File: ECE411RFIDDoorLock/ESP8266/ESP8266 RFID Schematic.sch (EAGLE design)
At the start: 30 parts, among them M1 SERVO, Q3 DMG341, T1 600mA/40V, T2 600mA/40V, U3 AP2112-3.3, X1 ESP-12E, X4 20329

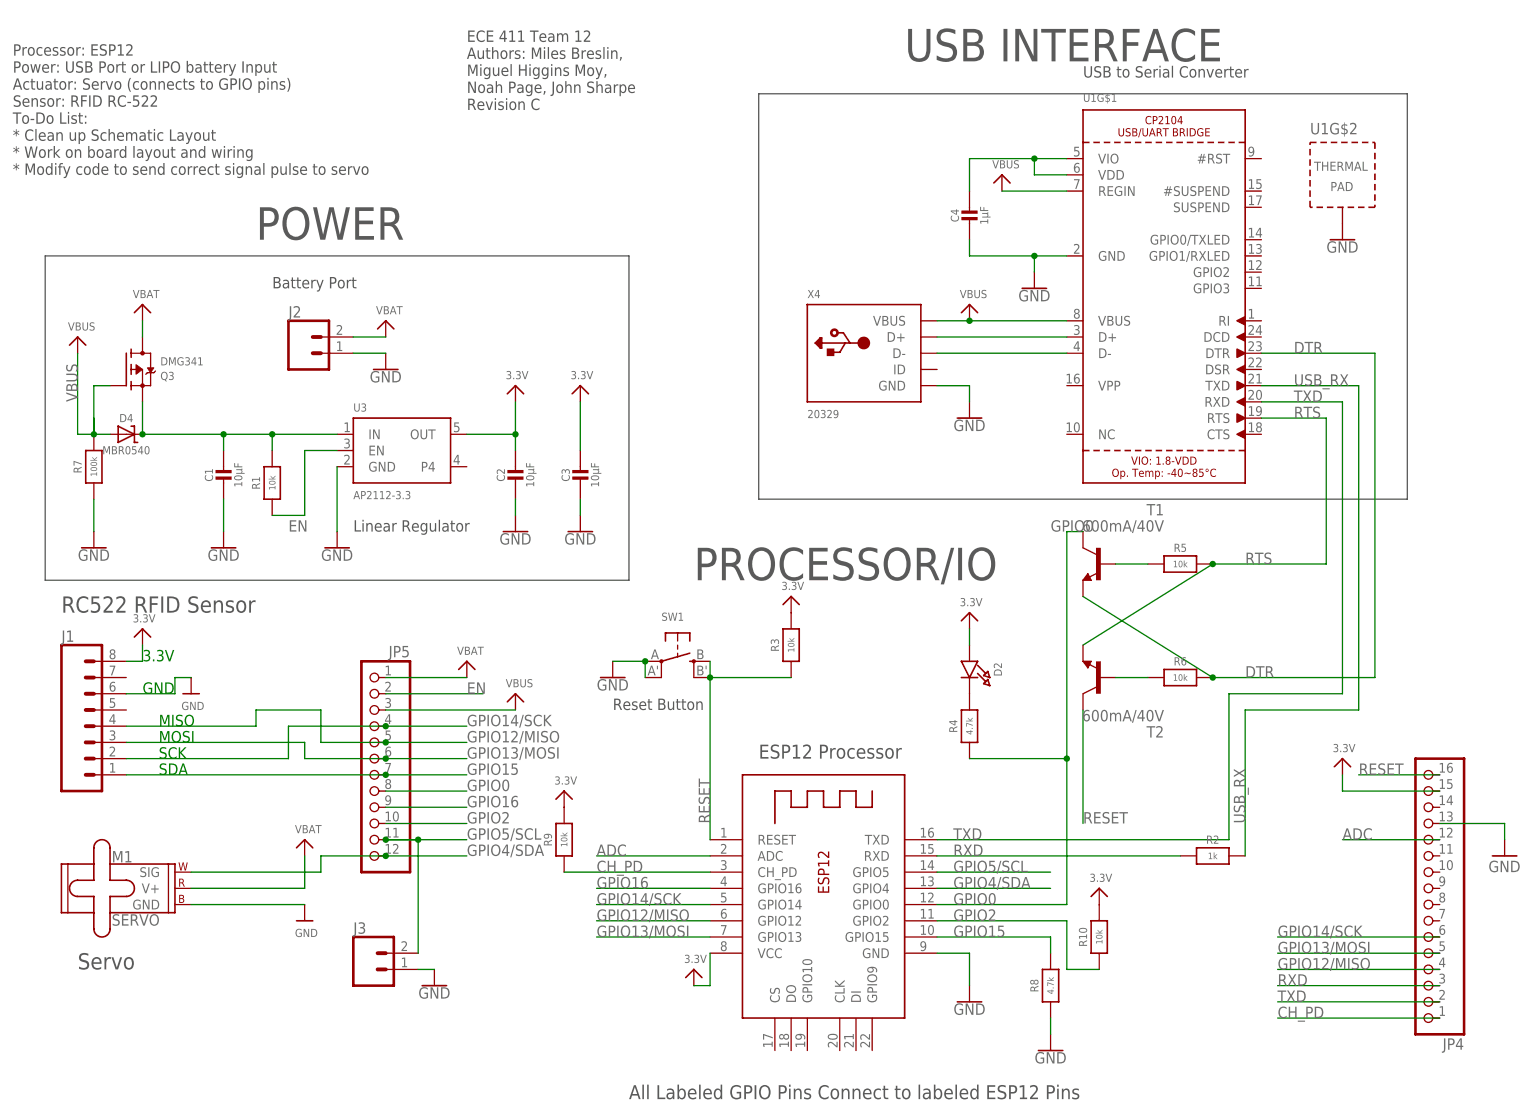
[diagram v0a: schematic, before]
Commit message: Design review feedback changed, USB replaced add new library
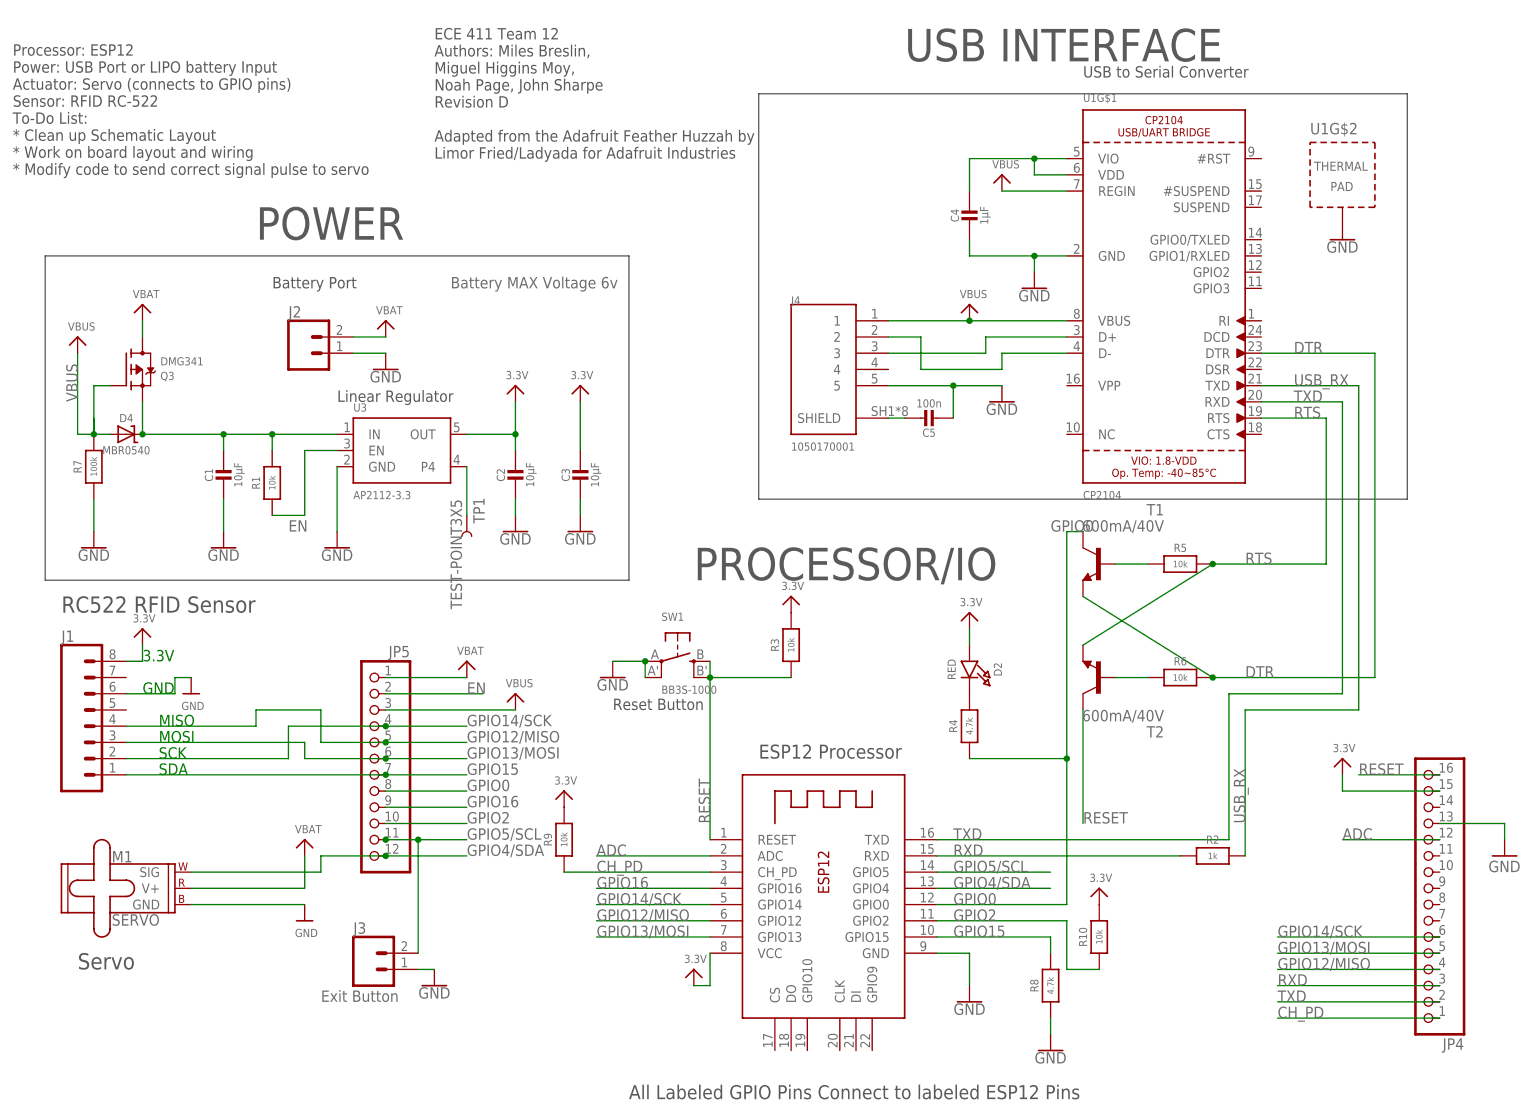
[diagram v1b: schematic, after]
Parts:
- removed X4: 20329, microbuilder:USB_MICRO_20329_V2
- added C5: 100n, microbuilder:CAP_CERAMIC0603MINI
- added J4: 1050170001, 1050170001:1050170001
- added TP1: TEST-POINT3X5, SparkFun-Connectors:TEST-POINT3X5
- D2: value (none) -> RED
- SW1: value (none) -> BB3S-1000
- U1: value (none) -> CP2104
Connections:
- new net N$1: C5.1, J4.SHIELD
- new net N$2: J4.3, U1G$1.D+
- net GND: now also C5.2, J4.5; no longer X4.GND
- net N$3: now also J4.2, U1G$1.D-; no longer U1G$1.D+, X4.D+
- net N$4: now also TP1.1, U3.P4; no longer U1G$1.D-, X4.D-
- net VBUS: now also J4.1; no longer X4.VBUS
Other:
- note added: "Battery MAX Voltage 6v"
- note added: "ECE 411 Team 12 Authors: Miles Breslin, Miguel Higgins Moy, Noah Page, John Sharpe Revision D Adapted from the Adafruit Feather Huzzah by Limor Fried/Ladyada for Adafruit Industries"
- note added: "Exit Button"
- note removed: "ECE 411 Team 12 Authors: Miles Breslin, Miguel Higgins Moy, Noah Page, John Sharpe Revision C"

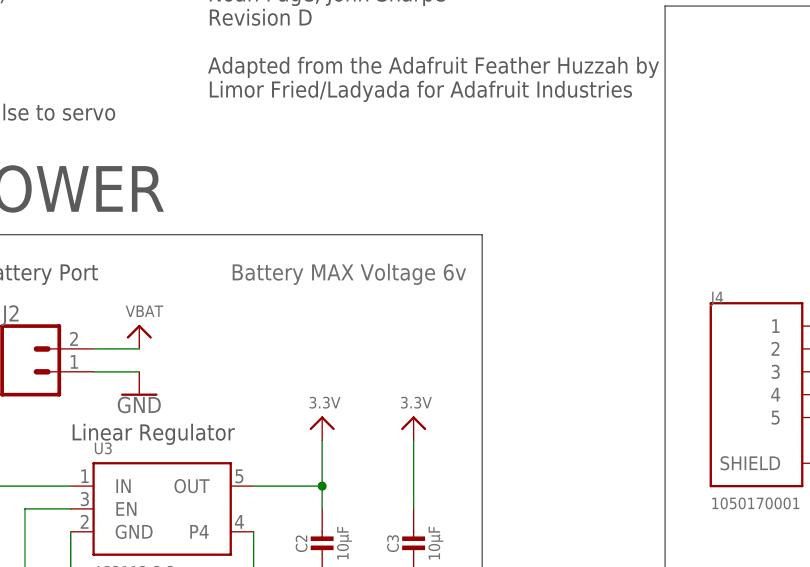
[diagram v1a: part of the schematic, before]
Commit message: PCB Clean Up from Design Review
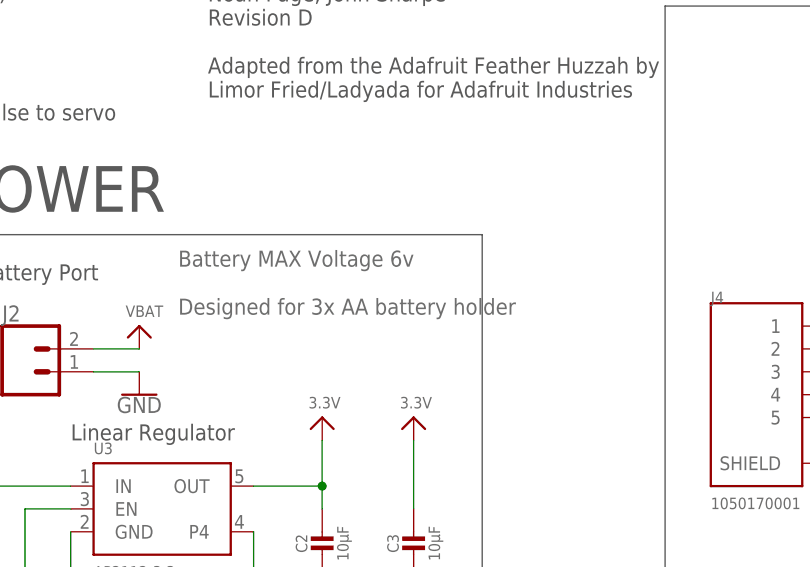
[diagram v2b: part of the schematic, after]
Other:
- note added: "Battery MAX Voltage 6v Designed for 3x AA battery holder"
- note removed: "Battery MAX Voltage 6v"
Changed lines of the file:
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@@
 <grid distance="0.1" unitdist="inch" unit="inch" style="lines" multiple="1" display="no" altdistance="0.01" altunitdist="inch" altunit="inch"/>
 <layers>
-<layer number="1" name="Top" color="4" fill="1" visible="yes" active="no"/>
-<layer number="2" name="Route2" color="16" fill="1" visible="yes" active="no"/>
-<layer number="3" name="Route3" color="17" fill="1" visible="yes" active="no"/>
-<layer number="4" name="Route4" color="18" fill="1" visible="yes" active="no"/>
-<layer number="5" name="Route5" color="19" fill="1" visible="yes" active="no"/>
-<layer number="6" name="Route6" color="25" fill="1" visible="yes" active="no"/>
-<layer number="7" name="Route7" color="26" fill="1" visible="yes" active="no"/>
-<layer number="8" name="Route8" color="27" fill="1" visible="yes" active="no"/>
-<layer number="9" name="Route9" color="28" fill="1" visible="yes" active="no"/>
-<layer number="10" name="Route10" color="29" fill="1" visible="yes" active="no"/>
-<layer number="11" name="Route11" color="30" fill="1" visible="yes" active="no"/>
-<layer number="12" name="Route12" color="20" fill="1" visible="yes" active="no"/>
-<layer number="13" name="Route13" color="21" fill="1" visible="yes" active="no"/>
-<layer number="14" name="Route14" color="22" fill="1" visible="yes" active="no"/>
-<layer number="15" name="Route15" color="23" fill="1" visible="yes" active="no"/>
-<layer number="16" name="Bottom" color="1" fill="1" visible="yes" active="no"/>
-<layer number="17" name="Pads" color="2" fill="1" visible="yes" active="no"/>
-<layer number="18" name="Vias" color="2" fill="1" visible="yes" active="no"/>
-<layer number="19" name="Unrouted" color="6" fill="1" visible="yes" active="no"/>
-<layer number="20" name="Dimension" color="24" fill="1" visible="yes" active="no"/>
-<layer number="21" name="tPlace" color="7" fill="1" visible="yes" active="no"/>
-<layer number="22" name="bPlace" color="7" fill="1" visible="yes" active="no"/>
-<layer number="23" name="tOrigins" color="15" fill="1" visible="yes" active="no"/>
-<layer number="24" name="bOrigins" color="15" fill="1" visible="yes" active="no"/>
-<layer number="25" name="tNames" color="7" fill="1" visible="yes" active="no"/>
-<layer number="26" name="bNames" color="7" fill="1" visible="yes" active="no"/>
-<layer number="27" name="tValues" color="7" fill="1" visible="yes" active="no"/>
-<layer number="28" name="bValues" color="7" fill="1" visible="yes" active="no"/>
+<layer number="1" name="Top" color="4" fill="1" visible="no" active="no"/>
+<layer number="2" name="Route2" color="16" fill="1" visible="no" active="no"/>
+<layer number="3" name="Route3" color="17" fill="1" visible="no" active="no"/>
+<layer number="4" name="Route4" color="18" fill="1" visible="no" active="no"/>
+<layer number="5" name="Route5" color="19" fill="1" visible="no" active="no"/>
+<layer number="6" name="Route6" color="25" fill="1" visible="no" active="no"/>
+<layer number="7" name="Route7" color="26" fill="1" visible="no" active="no"/>
+<layer number="8" name="Route8" color="27" fill="1" visible="no" active="no"/>
+<layer number="9" name="Route9" color="28" fill="1" visible="no" active="no"/>
+<layer number="10" name="Route10" color="29" fill="1" visible="no" active="no"/>
+<layer number="11" name="Route11" color="30" fill="1" visible="no" active="no"/>
+<layer number="12" name="Route12" color="20" fill="1" visible="no" active="no"/>
+<layer number="13" name="Route13" color="21" fill="1" visible="no" active="no"/>
+<layer number="14" name="Route14" color="22" fill="1" visible="no" active="no"/>
+<layer number="15" name="Route15" color="23" fill="1" visible="no" active="no"/>
+<layer number="16" name="Bottom" color="1" fill="1" visible="no" active="no"/>
+<layer number="17" name="Pads" color="2" fill="1" visible="no" active="no"/>
+<layer number="18" name="Vias" color="2" fill="1" visible="no" active="no"/>
+<layer number="19" name="Unrouted" color="6" fill="1" visible="no" active="no"/>
+<layer number="20" name="Dimension" color="24" fill="1" visible="no" active="no"/>
+<layer number="21" name="tPlace" color="7" fill="1" visible="no" active="no"/>
+<layer number="22" name="bPlace" color="7" fill="1" visible="no" active="no"/>
+<layer number="23" name="tOrigins" color="15" fill="1" visible="no" active="no"/>
+<layer number="24" name="bOrigins" color="15" fill="1" visible="no" active="no"/>
+<layer number="25" name="tNames" color="7" fill="1" visible="no" active="no"/>
+<layer number="26" name="bNames" color="7" fill="1" visible="no" active="no"/>
+<layer number="27" name="tValues" color="7" fill="1" visible="no" active="no"/>
+<layer number="28" name="bValues" color="7" fill="1" visible="no" active="no"/>
 <layer number="29" name="tStop" color="7" fill="3" visible="no" active="no"/>
 <layer number="30" name="bStop" color="7" fill="6" visible="no" active="no"/>
@@
 <layer number="35" name="tGlue" color="7" fill="4" visible="no" active="no"/>
 <layer number="36" name="bGlue" color="7" fill="5" visible="no" active="no"/>
-<layer number="37" name="tTest" color="7" fill="1" visible="yes" active="no"/>
-<layer number="38" name="bTest" color="7" fill="1" visible="yes" active="no"/>
+<layer number="37" name="tTest" color="7" fill="1" visible="no" active="no"/>
+<layer number="38" name="bTest" color="7" fill="1" visible="no" active="no"/>
 <layer number="39" name="tKeepout" color="4" fill="11" visible="no" active="no"/>
 <layer number="40" name="bKeepout" color="1" fill="11" visible="no" active="no"/>
@@
 <layer number="44" name="Drills" color="7" fill="1" visible="no" active="no"/>
 <layer number="45" name="Holes" color="7" fill="1" visible="no" active="no"/>
-<layer number="46" name="Milling" color="3" fill="1" visible="yes" active="no"/>
-<layer number="47" name="Measures" color="7" fill="1" visible="yes" active="no"/>
-<layer number="48" name="Document" color="7" fill="1" visible="yes" active="no"/>
-<layer number="49" name="Reference" color="7" fill="1" visible="yes" active="no"/>
-<layer number="50" name="dxf" color="7" fill="1" visible="yes" active="no"/>
-<layer number="51" name="tDocu" color="7" fill="1" visible="yes" active="no"/>
-<layer number="52" name="bDocu" color="7" fill="1" visible="yes" active="no"/>
-<layer number="53" name="tGND_GNDA" color="7" fill="9" visible="yes" active="no"/>
-<layer number="54" name="bGND_GNDA" color="1" fill="9" visible="yes" active="no"/>
-<layer number="56" name="wert" color="7" fill="1" visible="yes" active="no"/>
-<layer number="57" name="tCAD" color="7" fill="1" visible="yes" active="no"/>
-<layer number="58" name="b3D" color="7" fill="1" visible="yes" active="no"/>
-<layer number="59" name="tCarbon" color="7" fill="1" visible="yes" active="no"/>
-<layer number="60" name="bCarbon" color="7" fill="1" visible="yes" active="no"/>
-<layer number="61" name="stand" color="7" fill="1" visible="yes" active="no"/>
+<layer number="46" name="Milling" color="3" fill="1" visible="no" active="no"/>
+<layer number="47" name="Measures" color="7" fill="1" visible="no" active="no"/>
+<layer number="48" name="Document" color="7" fill="1" visible="no" active="no"/>
+<layer number="49" name="Reference" color="7" fill="1" visible="no" active="no"/>
+<layer number="50" name="dxf" color="7" fill="1" visible="no" active="no"/>
+<layer number="51" name="tDocu" color="7" fill="1" visible="no" active="no"/>
+<layer number="52" name="bDocu" color="7" fill="1" visible="no" active="no"/>
+<layer number="53" name="tGND_GNDA" color="7" fill="9" visible="no" active="no"/>
+<layer number="54" name="bGND_GNDA" color="1" fill="9" visible="no" active="no"/>
+<layer number="56" name="wert" color="7" fill="1" visible="no" active="no"/>
+<layer number="57" name="tCAD" color="7" fill="1" visible="no" active="no"/>
+<layer number="58" name="b3D" color="7" fill="1" visible="no" active="no"/>
+<layer number="59" name="tCarbon" color="7" fill="1" visible="no" active="no"/>
+<layer number="60" name="bCarbon" color="7" fill="1" visible="no" active="no"/>
+<layer number="61" name="stand" color="7" fill="1" visible="no" active="no"/>
 <layer number="88" name="SimResults" color="9" fill="1" visible="yes" active="yes"/>
 <layer number="89" name="SimProbes" color="9" fill="1" visible="yes" active="yes"/>
@@
 <wire x1="228.6" y1="99.06" x2="228.6" y2="162.56" width="0.1524" layer="97"/>
 <wire x1="228.6" y1="162.56" x2="127" y2="162.56" width="0.1524" layer="97"/>
-<text x="78.74" y="132.08" size="1.778" layer="95">Battery MAX Voltage 6v</text>
+<text x="72.898" y="128.27" size="1.778" layer="95">Battery MAX Voltage 6v
+Designed for 3x AA battery holder</text>
 <text x="58.42" y="20.32" size="1.778" layer="95">Exit Button</text>
 </plain>

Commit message: Final PCB Draft, some component modifications, please take a look.
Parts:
- removed SW1: BB3S-1000, microbuilder:SWITCH_TACT_SMT
- removed TP1: TEST-POINT3X5, SparkFun-Connectors:TEST-POINT3X5
- removed U3: AP2112-3.3, microbuilder:VREG_SOT23-5
- added S1: B3S-1000, B3S-1000:B3S-1000
- added U2: AP2112K-3.3TRG1, AP2112K-3.3TRG1:AP2112K-3.3TRG1
- D4: value MBR0540 -> MBR140SFT1G
- Q3: value DMG341 -> MMBT2222ALT1GOSCT-ND
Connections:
- removed net N$4: TP1.1, U3.P4
- net 3.3V: now also U2.VOUT; no longer U3.OUT
- net EN: now also U2.EN; no longer U3.EN
- net GND: now also S1.COM, U2.GND; no longer SW1.P, SW1.P1, U3.GND
- net N$8: now also U2.VIN; no longer U3.IN
- net RESET: now also S1.NO; no longer SW1.S, SW1.S1
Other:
- moved on the sheet: R3

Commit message: Final PCB draft
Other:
- note added: "ECE 411 Team 12 Authors: Miles Breslin, Miguel Higgins Moy, Noah Page, John Sharpe Revision E Adapted from the Adafruit Feather Huzzah by Limor Fried/Ladyada for Adafruit Industries"
- note added: "Processor: ESP12 Power: USB Port or 3x AA battery Actuator: Servo (connects to GPIO pins) Sensor: RFID RC-522"
- note removed: "ECE 411 Team 12 Authors: Miles Breslin, Miguel Higgins Moy, Noah Page, John Sharpe Revision D Adapted from the Adafruit Feather Huzzah by Limor Fried/Ladyada for Adafruit Industries"
- note removed: "Processor: ESP12 Power: USB Port or LIPO battery Input Actuator: Servo (connects to GPIO pins) Sensor: RFID RC-522 To-Do List: * Clean up Schematic Layout * Work on board layout and wiring * Modify code to send correct signal pulse to servo"
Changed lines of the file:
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@@
 <text x="177.8" y="165.1" size="1.778" layer="97">USB to Serial Converter</text>
 <text x="10.16" y="149.86" size="1.778" layer="97">Processor: ESP12
-Power: USB Port or LIPO battery Input
+Power: USB Port or 3x AA battery
 Actuator: Servo (connects to GPIO pins)
 Sensor: RFID RC-522
-To-Do List:
-* Clean up Schematic Layout
-* Work on board layout and wiring
-* Modify code to send correct signal pulse to servo
 </text>
 <text x="48.26" y="139.7" size="5.08" layer="97">POWER</text>
@@
 Miguel Higgins Moy,
 Noah Page, John Sharpe
-Revision D
+Revision E
 Adapted from the Adafruit Feather Huzzah by
 Limor Fried/Ladyada for Adafruit Industries</text>
